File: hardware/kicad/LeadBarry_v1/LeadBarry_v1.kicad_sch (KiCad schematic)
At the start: 4 parts, among them U1 PicoW

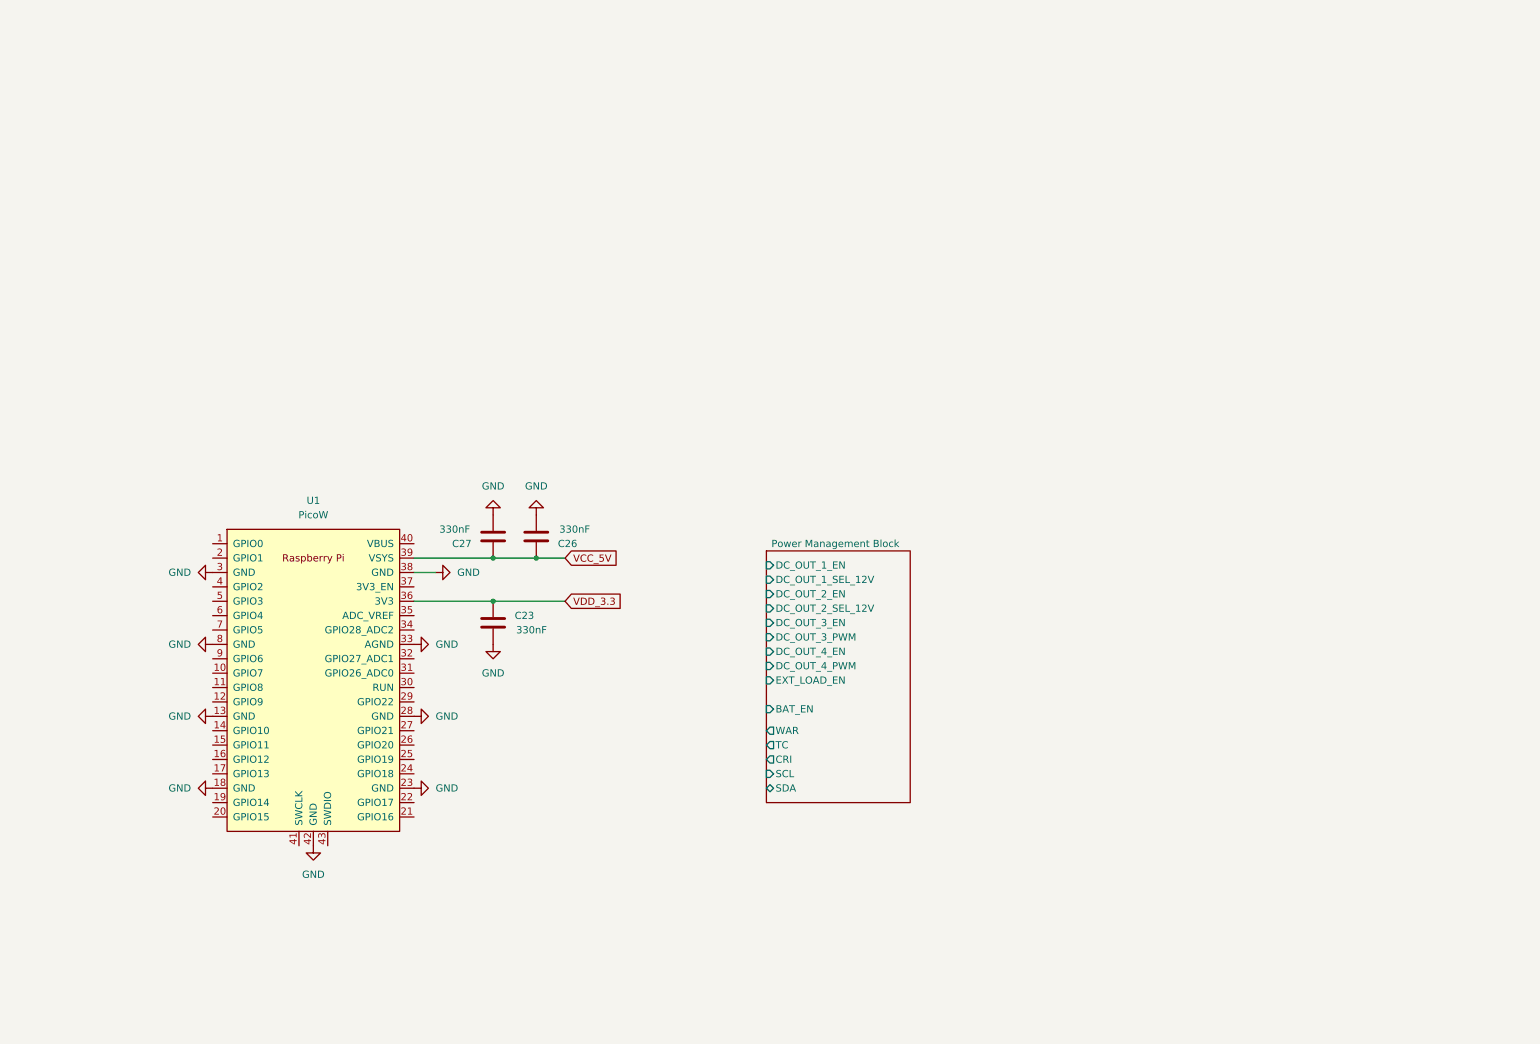
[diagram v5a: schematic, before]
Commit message: fix: added display and timer to the schematic
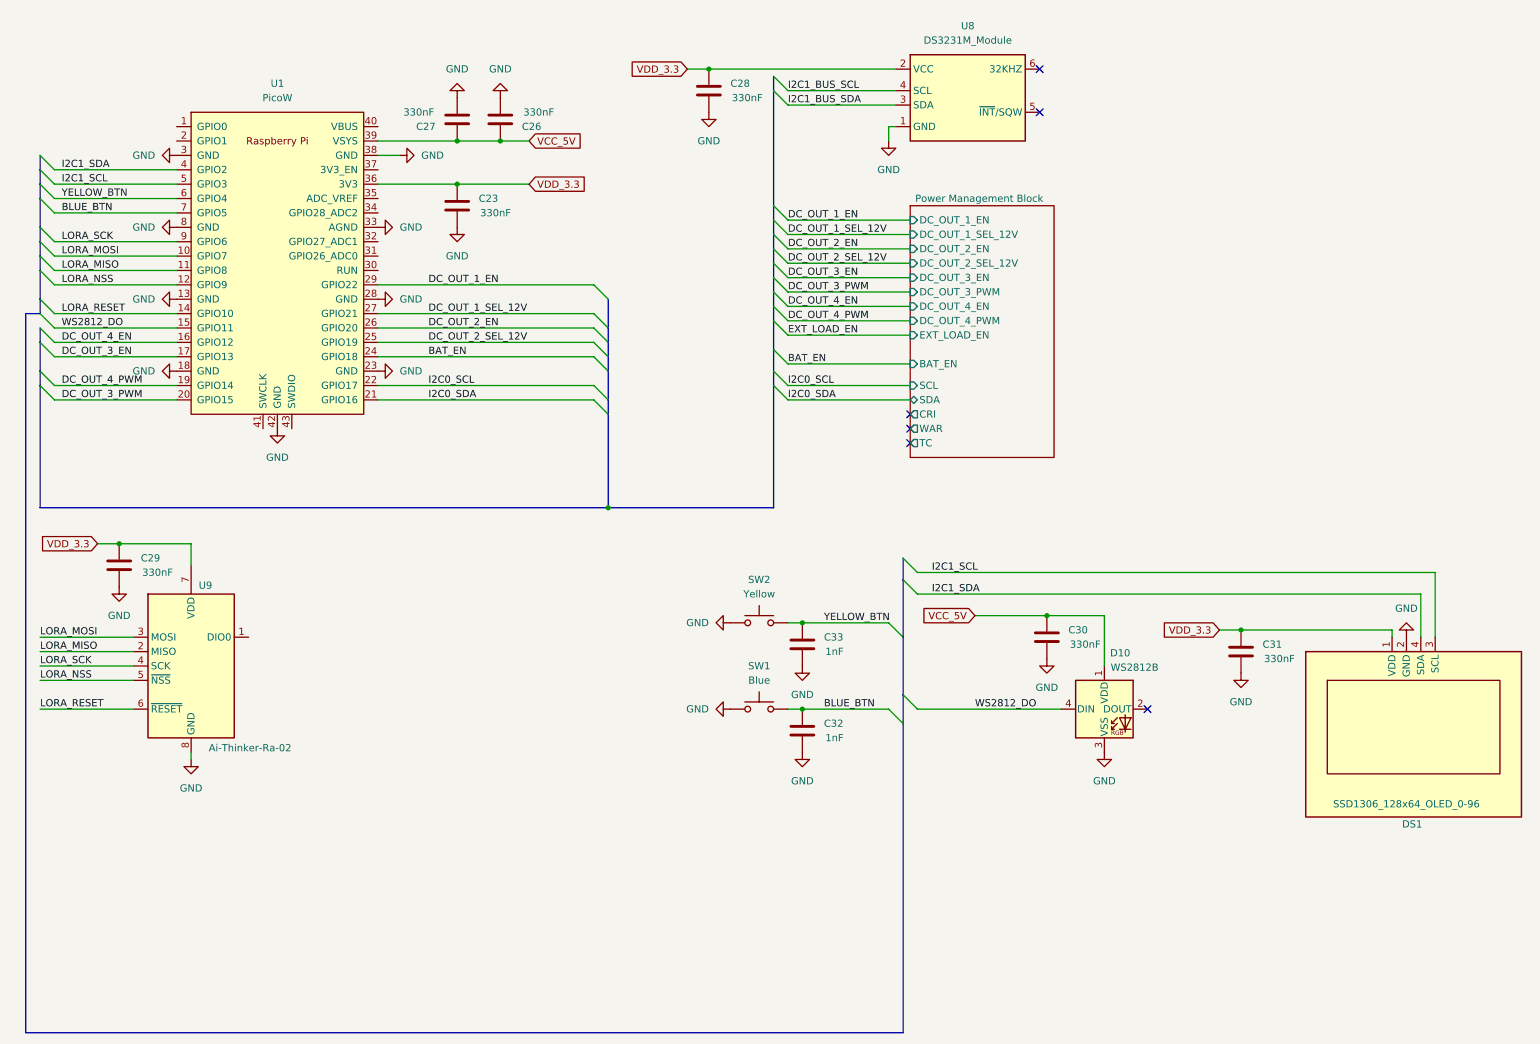
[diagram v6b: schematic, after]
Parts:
- added C28, C29, C30, C31: 330nF, Capacitor_SMD:C_1206_3216Metric_Pad1.33x1.80mm_HandSolder, symbol Device:C
- added C32, C33: 1nF, Capacitor_SMD:C_0805_2012Metric_Pad1.18x1.45mm_HandSolder, symbol Device:C
- added D10: WS2812B, LED_SMD:LED_WS2812B_PLCC4_5.0x5.0mm_P3.2mm, symbol LED:WS2812B
- added DS1: SSD1306_128x64_OLED_0-96, Display:SSD1306_128x64_OLED_096_Display, symbol Display_Graphic:SSD1306_128x64_OLED_0-96
- added SW1: Blue, Button_Switch_SMD:SW_SPST_CK_KMS2xxGP, symbol Switch:SW_Push
- added SW2: Yellow, Button_Switch_SMD:SW_SPST_CK_KMS2xxGP, symbol Switch:SW_Push
- added U8: DS3231M_Module, Module:DS3231M_Module_Flat, symbol Timer_RTC:DS3231M_Module
- added U9: Ai-Thinker-Ra-02, RF_Module:Ai-Thinker-Ra-02_Module, symbol RF_Module:Ai-Thinker-Ra-02_Module
- U1: footprint RPi_PicoW:RPi_Pico_SMD_TH -> RPi_PicoW:RPi_PicoW_SMD_TH
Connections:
- net GND: now also C28.2, C29.2, C30.2, C31.2, C32.2, C33.2, D10.3 (VSS), DS1.2 (GND), SW1.1, SW2.1, U8.1 (GND), U9.8 (GND)
- net VCC_5V: now also C30.1, D10.1 (VDD)
- net VDD_3.3: now also C28.1, C29.1, C31.1, DS1.1 (VDD), U8.2 (VCC), U9.7 (VDD)
- net LORA_MOSI: now reaches U1.10 (GPIO7)
- net LORA_MOSI: now also U9.3 (MOSI)
- net LORA_MISO: now reaches U1.11 (GPIO8)
- net LORA_MISO: now also U9.2 (MISO)
- net LORA_NSS: now reaches U1.12 (GPIO9)
- net LORA_NSS: now also U9.5 (~{NSS})
- net LORA_RESET: now reaches U1.14 (GPIO10)
- net LORA_RESET: now also U9.6 (~{RESET})
- net WS2812_DO: now reaches U1.15 (GPIO11)
- net WS2812_DO: now also D10.4 (DIN)
- net DC_OUT_4_EN: now reaches U1.16 (GPIO12)
- net DC_OUT_3_EN: now reaches U1.17 (GPIO13)
- net DC_OUT_4_PWM: now reaches U1.19 (GPIO14)
- net DC_OUT_3_PWM: now reaches U1.20 (GPIO15)
- net I2C0_SDA: now reaches U1.21 (GPIO16)
- net I2C0_SCL: now reaches U1.22 (GPIO17)
- net BAT_EN: now reaches U1.24 (GPIO18)
- net DC_OUT_2_SEL_12V: now reaches U1.25 (GPIO19)
- net DC_OUT_2_EN: now reaches U1.26 (GPIO20)
- net DC_OUT_1_SEL_12V: now reaches U1.27 (GPIO21)
- net DC_OUT_1_EN: now reaches U1.29 (GPIO22)
- net I2C1_SDA: now reaches U1.4 (GPIO2)
- net I2C1_SDA: now also DS1.4 (SDA)
- net I2C1_SCL: now reaches U1.5 (GPIO3)
- net I2C1_SCL: now also DS1.3 (SCL)
- net YELLOW_BTN: now reaches U1.6 (GPIO4)
- net YELLOW_BTN: now also C33.1, SW2.2
- net BLUE_BTN: now reaches U1.7 (GPIO5)
- net BLUE_BTN: now also C32.1, SW1.2
- net LORA_SCK: now reaches U1.9 (GPIO6)
- net LORA_SCK: now also U9.4 (SCK)
- new net I2C1_BUS_SCL: U8.4 (SCL)
- new net I2C1_BUS_SDA: U8.3 (SDA)
- no-connect marks 0 -> 6
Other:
- title: (none) -> Main Board
- moved on the sheet: C23, C26, C27, U1

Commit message: fix: reorganized circuitry
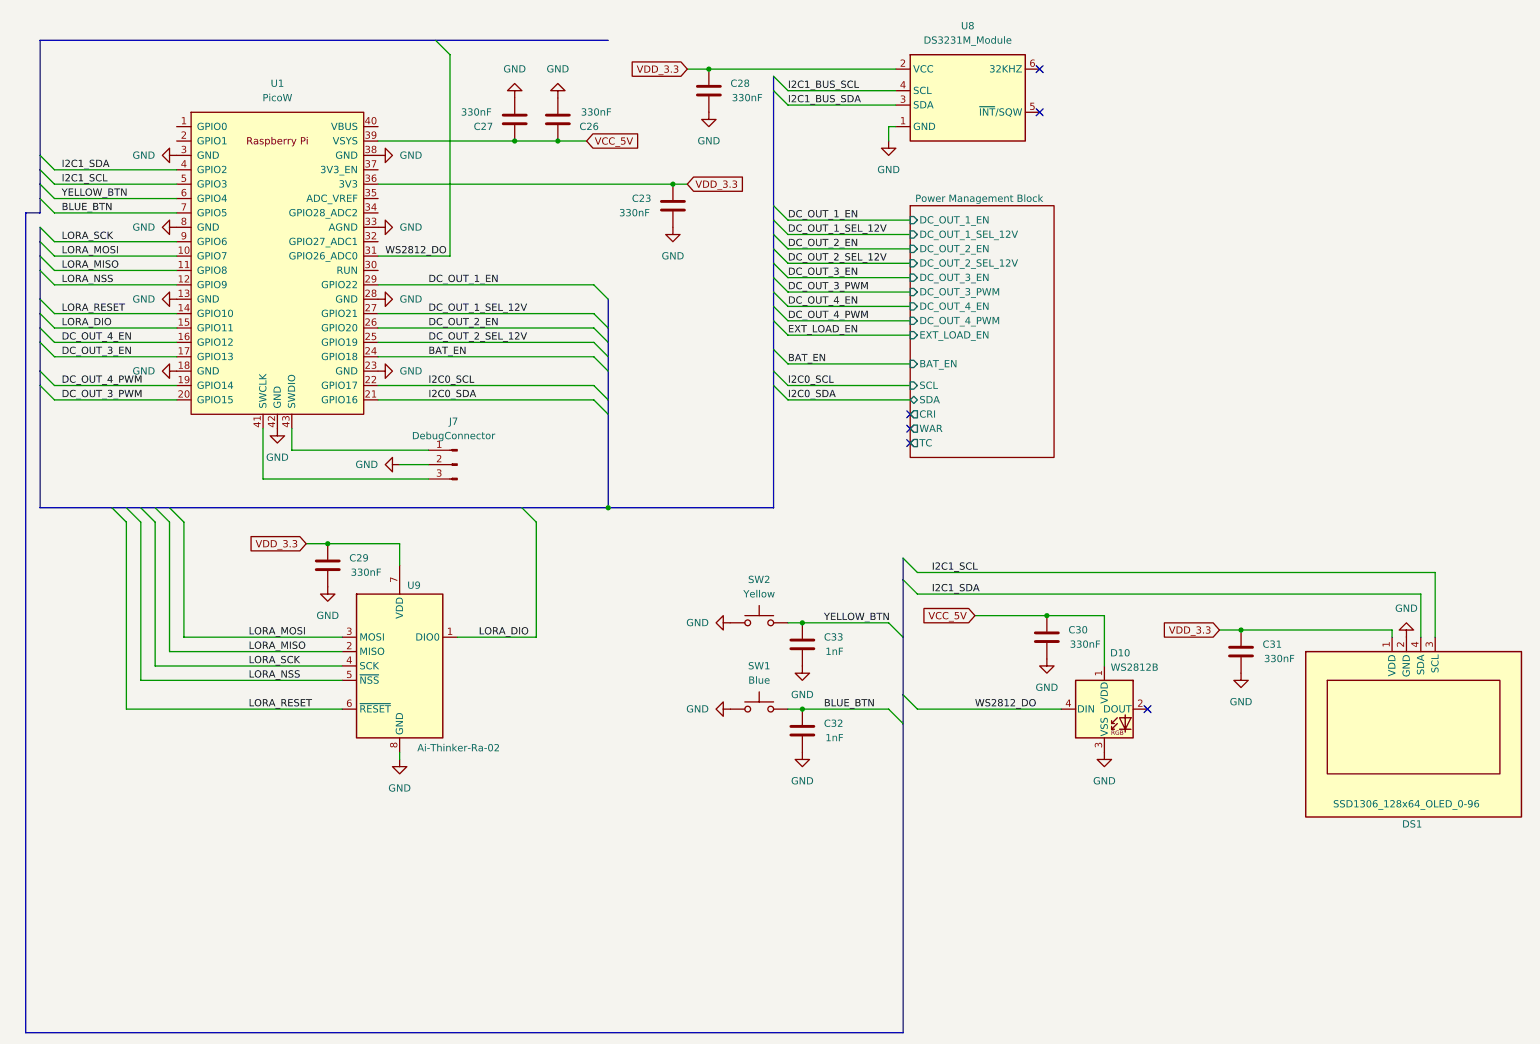
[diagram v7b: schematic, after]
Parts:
- added J7: DebugConnector, Connector_PinHeader_2.54mm:PinHeader_1x03_P2.54mm_Horizontal, symbol Connector:Conn_01x03_Pin
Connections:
- net GND: now also J7.2 (Pin_2)
- net WS2812_DO: now also U1.31 (GPIO26_ADC0); no longer U1.15 (GPIO11)
- net at U1.41 (SWCLK): now also J7.3 (Pin_3)
- net at U1.43 (SWDIO): now also J7.1 (Pin_1)
- net LORA_DIO: now reaches U9.1 (DIO0)
- net LORA_DIO: now also U1.15 (GPIO11)
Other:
- moved on the sheet: C23, C26, C27, C29, U9

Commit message: fix: RS485 port schematic implemented. Added shift+latch register as a port extension to control the DC outputs.
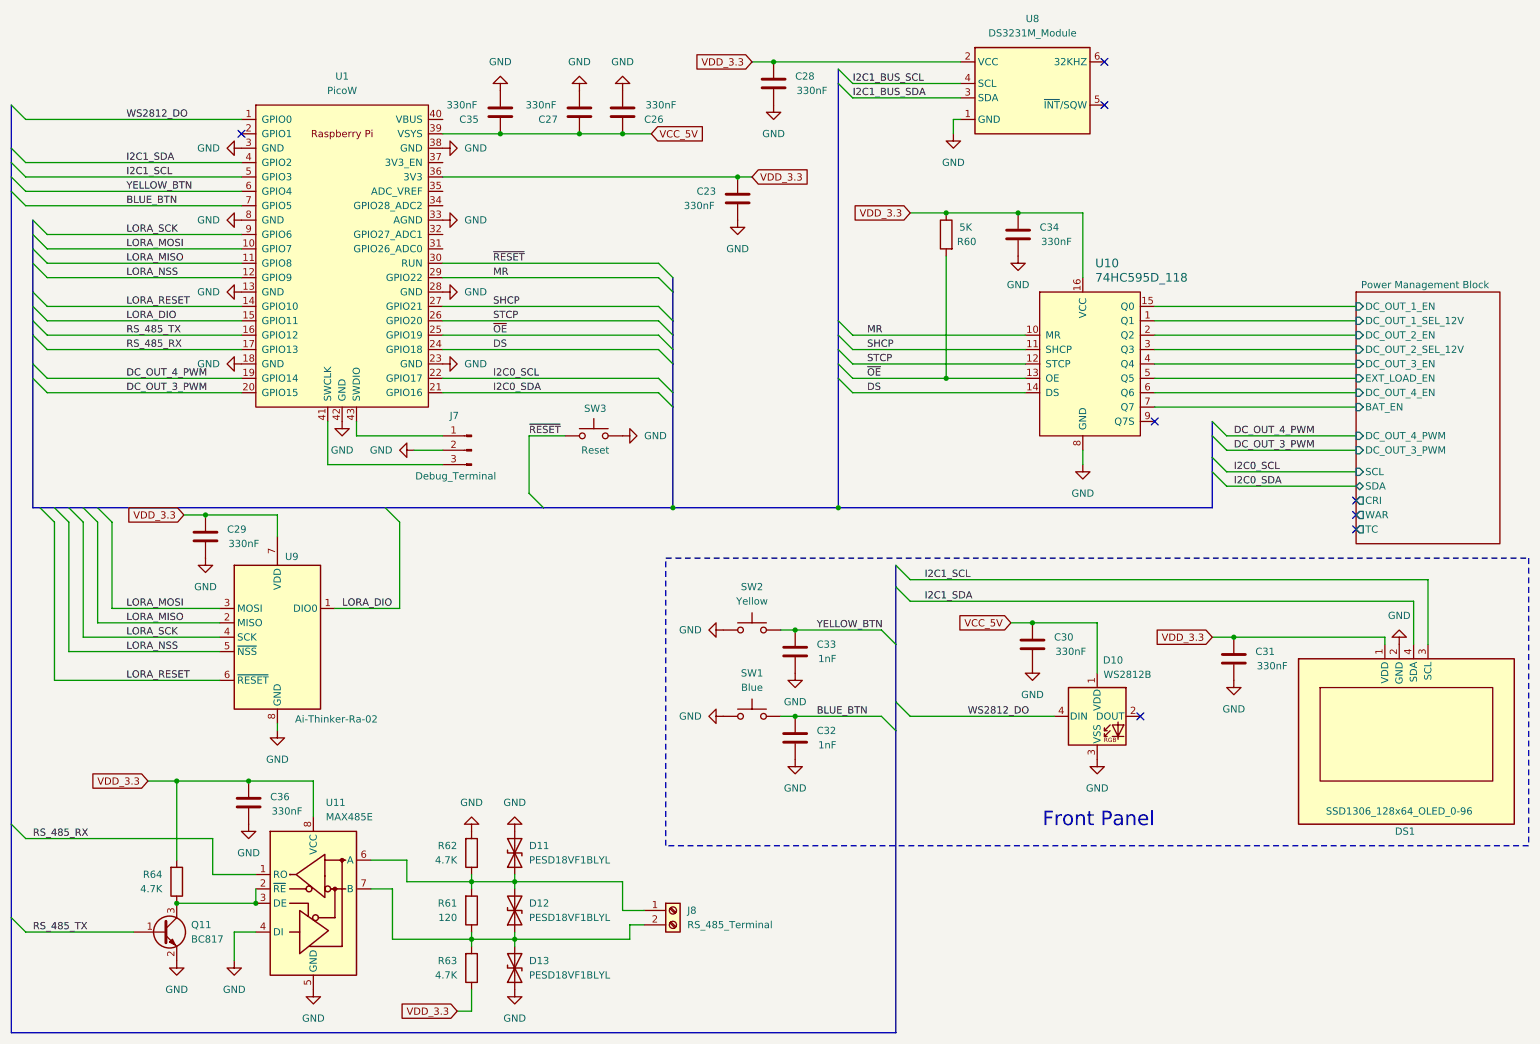
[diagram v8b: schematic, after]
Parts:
- added C34, C35, C36: 330nF, Capacitor_SMD:C_1206_3216Metric_Pad1.33x1.80mm_HandSolder, symbol Device:C
- added D11, D12, D13: PESD18VF1BLYL, Diode_SMD:D_SOD-882D, symbol Device:D_TVS
- added J8: RS_485_Terminal, TerminalBlock_Phoenix:TerminalBlock_Phoenix_MKDS-1,5-2-5.08_1x02_P5.08mm_Horizontal, symbol Connector:Screw_Terminal_01x02
- added Q11: BC817, Package_TO_SOT_SMD:SOT-23, symbol Transistor_BJT:BC817
- added R60: 5K, Resistor_SMD:R_0805_2012Metric_Pad1.20x1.40mm_HandSolder, symbol Device:R
- added R61: 120, Resistor_SMD:R_0805_2012Metric_Pad1.20x1.40mm_HandSolder, symbol Device:R
- added R62, R63, R64: 4.7K, Resistor_SMD:R_0805_2012Metric_Pad1.20x1.40mm_HandSolder, symbol Device:R
- added SW3: Reset, Button_Switch_SMD:SW_SPST_CK_KMS2xxGP, symbol Switch:SW_Push
- added U10: 74HC595D_118, digikey-footprints:SOIC-16_W3.90mm, symbol dk_Logic-Shift-Registers:74HC595D_118
- added U11: MAX485E, symbol Interface_UART:MAX485E
- J7: value DebugConnector -> Debug_Terminal
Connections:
- net GND: now also C34.2, C35.2, C36.2, D11.2 (A2), D13.1 (A1), Q11.2 (E), R62.2, SW3.1, U10.8 (GND), U11.4 (DI), U11.5 (GND)
- net VCC_5V: now also C35.1
- net VDD_3.3: now also C34.1, C36.1, R60.1, R63.1, R64.2, U10.16 (VCC), U11.8 (VCC)
- net WS2812_DO: now also U1.1 (GPIO0); no longer U1.31 (GPIO26_ADC0)
- net ~{RESET}: now reaches U1.30 (RUN)
- net ~{RESET}: now also SW3.2
- net BAT_EN renamed DS
- net DS: now also U10.14 (DS)
- net DC_OUT_1_EN renamed MR
- net MR: now also U10.10 (MR)
- net DC_OUT_1_SEL_12V renamed SHCP
- net SHCP: now also U10.11 (SHCP)
- net DC_OUT_2_EN renamed STCP
- net STCP: now also U10.12 (STCP)
- net DC_OUT_2_SEL_12V renamed ~{OE}
- net ~{OE}: now also R60.2, U10.13 (OE)
- net DC_OUT_3_EN renamed RS_485_RX
- net RS_485_RX: now also U11.1 (RO)
- net DC_OUT_4_EN renamed RS_485_TX
- net RS_485_TX: now also Q11.1 (B)
- new net: Q11.3 (C), R64.1, U11.2 (~{RE}), U11.3 (DE)
- new net: D11.1 (A1), D12.2 (A2), J8.1 (Pin_1), R61.2, R62.1, U11.6 (A)
- new net: D12.1 (A1), D13.2 (A2), J8.2 (Pin_2), R61.1, R63.2, U11.7 (B)
- new net PowerManagementBlock/BAT_EN: U10.7 (Q7)
- new net PowerManagementBlock/DC_OUT_1_EN: U10.15 (Q0)
- new net PowerManagementBlock/DC_OUT_1_SEL_12V: U10.1 (Q1)
- new net PowerManagementBlock/DC_OUT_2_EN: U10.2 (Q2)
- new net PowerManagementBlock/DC_OUT_2_SEL_12V: U10.3 (Q3)
- new net PowerManagementBlock/DC_OUT_3_EN: U10.4 (Q4)
- new net PowerManagementBlock/DC_OUT_4_EN: U10.6 (Q6)
- new net PowerManagementBlock/EXT_LOAD_EN: U10.5 (Q5)
- no-connect marks 6 -> 8
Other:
- note added: "Front Panel"
- moved on the sheet: C23, C26, C27, C28, C29, C30, C31, C32, C33, D10, DS1, J7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
